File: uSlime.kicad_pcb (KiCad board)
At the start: 2 copper layers, 25 x 22.6 mm, 32 parts, among them CN1 X1502WR-05K-N0SN, CN2 1.25T-2AW, J1 USB_C_Receptacle_USB2.0_14P, U1 ESP32-C6-MINI-1, U3 AP2112K-3.3TRG1, U4 MCP73831T-2ACI/OT, U5 BNO085, U6 MSK-12C02_SMD_SPDT_SWITCH, Y1 32.768

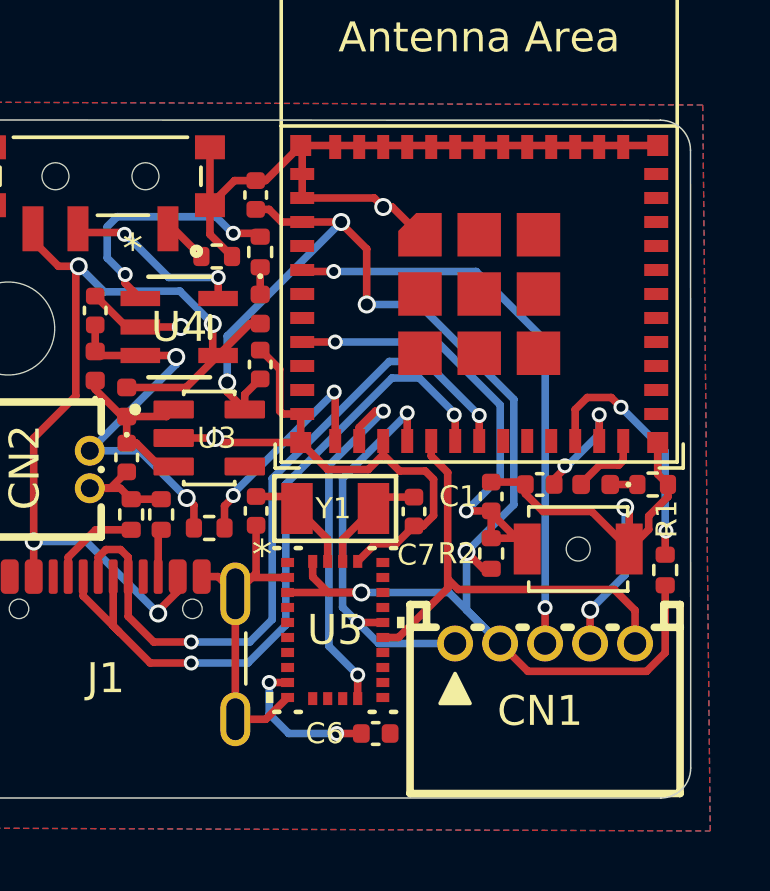
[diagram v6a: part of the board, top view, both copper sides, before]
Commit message: Add logo and remove crystal
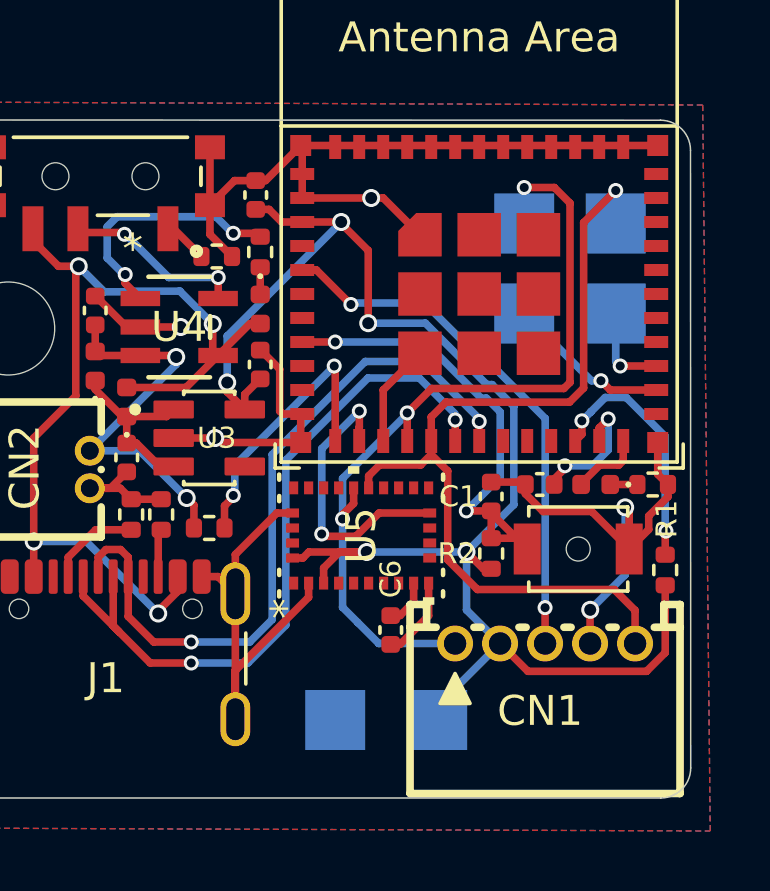
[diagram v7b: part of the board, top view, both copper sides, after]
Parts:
- removed C7, C8: 22pF, Capacitor_SMD:C_0402_1005Metric
- removed Y1: 32.768, uSlime-libs:OSC-SMD_L3.2-W1.5
- added G***: LOGO, uSlime-libs:uSlime_logo, B.Cu at (116.4, 100.0)
- added TP1: SDA, TestPoint:TestPoint_Pad_2.0x2.0mm, B.Cu at (120.1, 92.8)
- added TP2: SCL, TestPoint:TestPoint_Pad_2.0x2.0mm, B.Cu at (123.2, 92.8)
- added TP3: IO14, TestPoint:TestPoint_Pad_2.0x2.0mm, B.Cu at (120.1, 95.8)
- added TP4: IO14, TestPoint:TestPoint_Pad_2.0x2.0mm, B.Cu at (123.2, 95.8)
- added TP5: 3.3V, TestPoint:TestPoint_Pad_2.0x2.0mm, B.Cu at (117.2, 109.3)
- added TP6: GND, TestPoint:TestPoint_Pad_2.0x2.0mm, B.Cu at (113.8, 109.3)
- moved C6 3.49 mm to (115.7, 106.3), turned to 90 degrees
- moved U5 3.27 mm to (114.7, 103.2), turned to 90 degrees
- renumbered CHRG to CHRG1, RESET to RESET1, STAT to STAT1
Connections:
- U5 pad 26: Net-(U5-XOUT32/CLKSEL1) -> unconnected-(U5-XOUT32/CLKSEL1-Pad26)
- U5 pad 27: Net-(U5-XIN32) -> unconnected-(U5-XIN32-Pad27)
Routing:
- net BNO_SDA: track 13.4 -> 28.5 mm, vias 2 -> 3
- net BNO_SCL: track 15.8 -> 29.4 mm, vias 0 -> 1
- net /ESP32-C6FH4/IO20/PICO: track 0.00 -> 5.46 mm, vias 0 -> 1
- net Net-(U5-XIN32): track 3.72 -> 0.00 mm
- net Net-(U5-XOUT32/CLKSEL1): track 3.70 -> 0.00 mm
- net Net-(U5-CAP): track 5.00 -> 1.58 mm, vias 2 -> 0
- net /ESP32-C6FH4/IO21/POCI: track 0.00 -> 3.01 mm, vias 0 -> 1
- net BNO_INT: track 12.2 -> 9.57 mm
- net BatSense: track 7.76 -> 9.48 mm
- net +3.3V: track 50.5 -> 52.0 mm
- net BNO_INT2: track 19.2 -> 17.7 mm
- net GND: track 86.3 -> 85.1 mm
- net /ESP32-C6FH4/IO9/BOOT: track 3.79 -> 4.47 mm
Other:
- board text added: "ReSummit"
- board text added: "Slime"
